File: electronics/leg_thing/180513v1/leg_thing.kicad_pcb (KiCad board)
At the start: 2 copper layers, 39.4 x 62.2 mm, 8 parts, among them J1 HIP, J2 THIGH, J3 KNEE, J4 CALF, U1 ESP32THINGPOWERSHIELD, U2 Teensy3.2_no_outer_inner

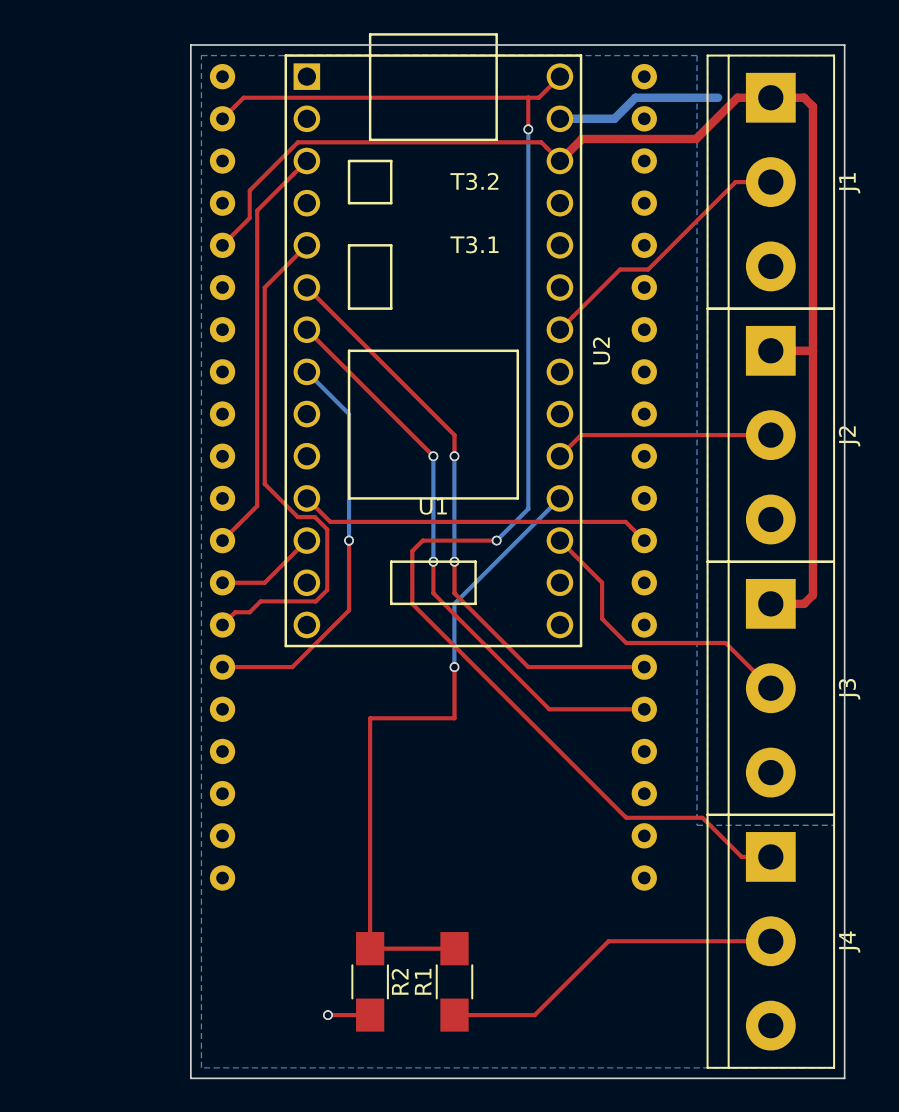
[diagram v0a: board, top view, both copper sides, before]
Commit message: reducing angular speed, setting max feet up to 1
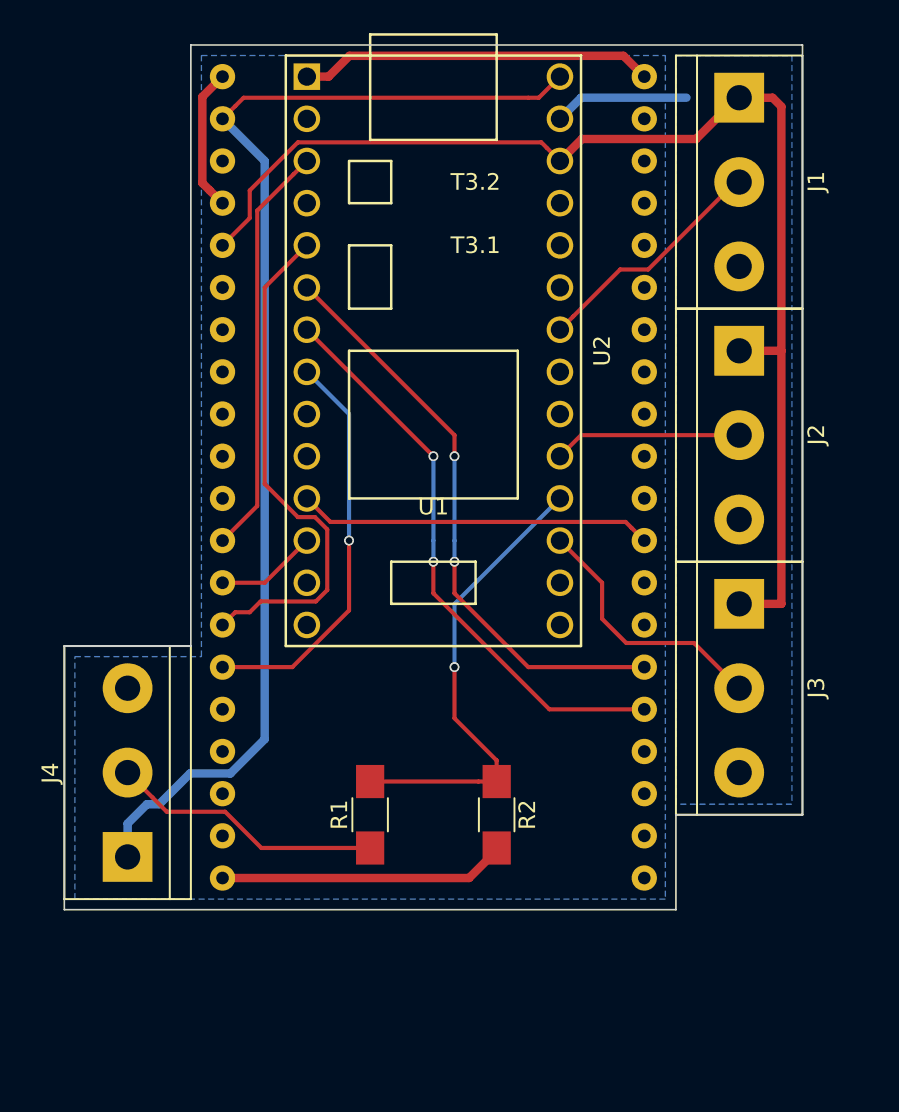
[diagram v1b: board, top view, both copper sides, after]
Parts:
- moved J4 38.7 mm to (95.9, 125.7), turned to 90 degrees
- moved R2 12.6 mm to (118.1, 123.2)
- moved R1 11.3 mm to (110.5, 123.2)
- moved J1 1.91 mm to (132.7, 80.0)
- moved J2 1.91 mm to (132.7, 95.2)
- moved J3 1.91 mm to (132.7, 110.5)
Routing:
- net GND: track 2.54 -> 47.3 mm, vias 1 -> 0
- net +5V: track 85.3 -> 72.2 mm, vias 2 -> 0
- net /CALFPOT3V3: track 39.9 -> 28.4 mm
- net /CALFPOT5V: track 20.9 -> 16.5 mm
- net /HIPPOT: track 16.4 -> 14.3 mm
- net /KNEEPOT: track 17.7 -> 15.8 mm
- net /THIGHPOT: track 13.2 -> 11.3 mm
- net GNDA: track 10.1 -> 8.15 mm
- net +3V3: track 76.1 -> 74.4 mm
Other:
- board size 39.4 x 62.2 mm -> 44.5 x 52.1 mm

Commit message: fixed esp32thingpowershield footprint, started new layout
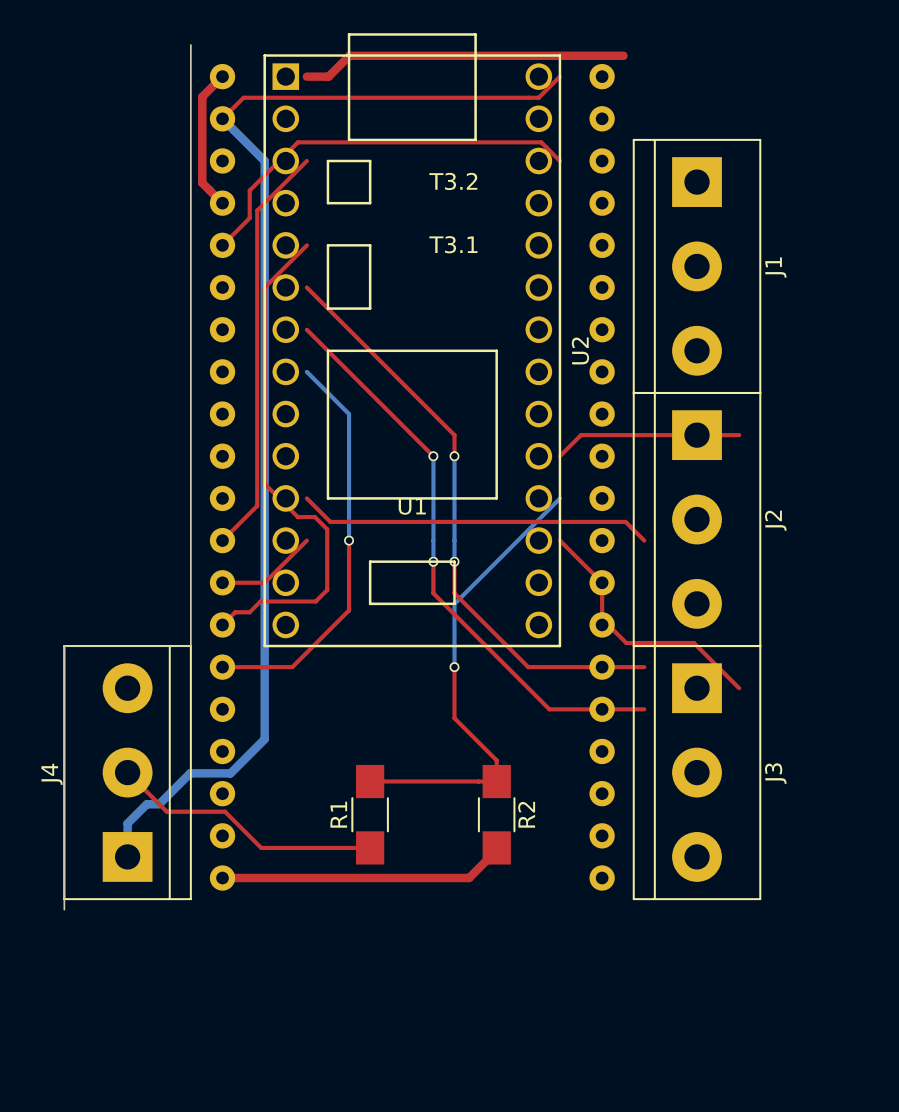
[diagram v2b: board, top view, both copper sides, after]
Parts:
- moved J1 5.68 mm to (130.2, 85.1)
- moved J2 5.68 mm to (130.2, 100.3)
- moved J3 5.68 mm to (130.2, 115.6)
- moved U1 1.27 mm to (113.0, 104.1)
- moved U2 1.27 mm to (113.0, 95.2)
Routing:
- net +3V3: track 74.4 -> 24.3 mm
- net /HIPPOT: track 14.3 -> 0.00 mm
- net (no net): track 0.00 -> 8.63 mm
- net GNDA: track 8.15 -> 0.00 mm
- net /KNEEPOT: track 15.8 -> 9.62 mm
- net GND: track 47.3 -> 43.1 mm
- removed copper zone on B.Cu, net GND
- removed copper zone on B.Cu, net GNDA
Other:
- board size 44.5 x 52.1 mm -> 7.6 x 52.1 mm

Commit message: electronics: switching to 6 pin molex connectors
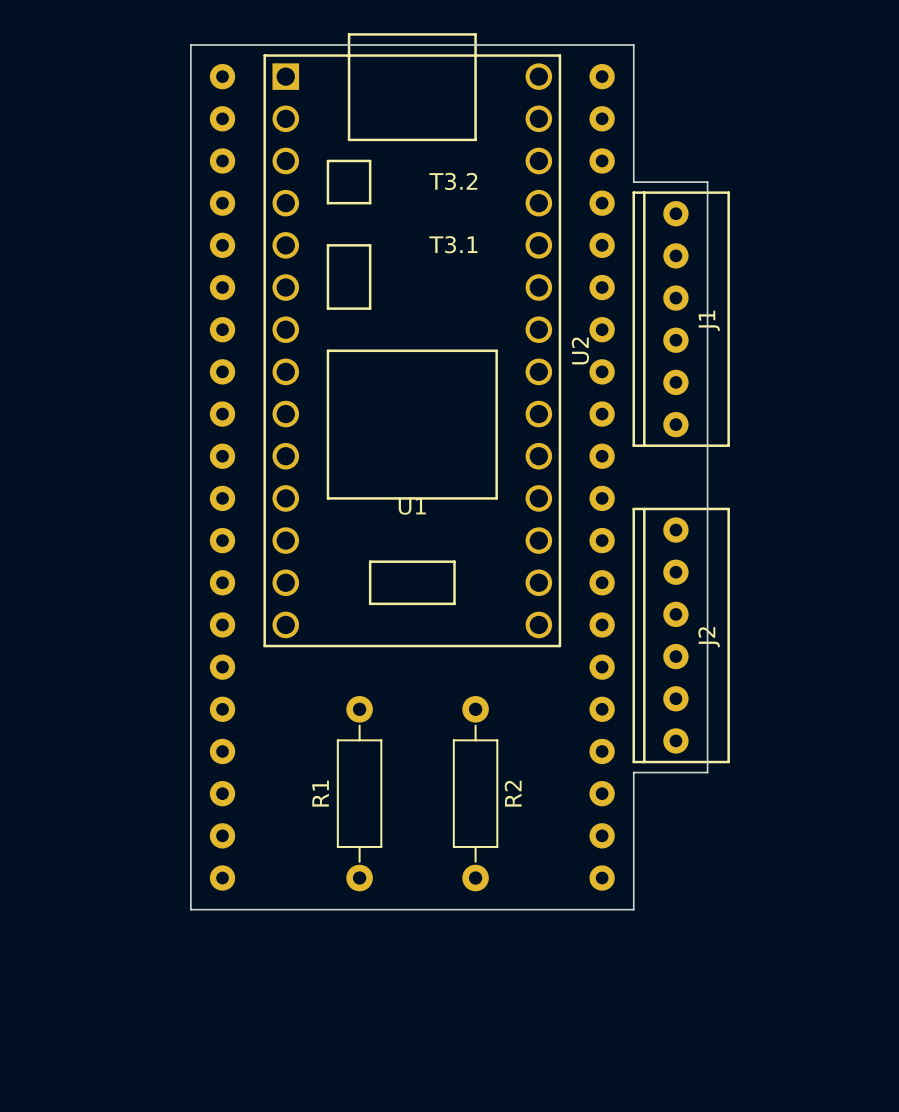
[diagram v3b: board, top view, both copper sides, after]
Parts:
- removed J3: KNEE, Connectors_Terminal_Blocks:TerminalBlock_bornier-3_P5.08mm
- removed J4: CALF, Connectors_Terminal_Blocks:TerminalBlock_bornier-3_P5.08mm
- J1: value HIP -> HIPCALF; footprint Connectors_Terminal_Blocks:TerminalBlock_bornier-3_P5.08mm -> leg_thing:MOLEX6PIN
- J2: value THIGH -> THIGHKNEE; footprint Connectors_Terminal_Blocks:TerminalBlock_bornier-3_P5.08mm -> leg_thing:MOLEX6PIN
- R1: value R -> 560; footprint Resistors_SMD:R_1206_HandSoldering -> Resistors_THT:R_Axial_DIN0207_L6.3mm_D2.5mm_P10.16mm_Horizontal
- R2: value R -> 1K; footprint Resistors_SMD:R_1206_HandSoldering -> Resistors_THT:R_Axial_DIN0207_L6.3mm_D2.5mm_P10.16mm_Horizontal
- moved J2 12.1 mm to (128.9, 112.4), turned to 0 degrees
- moved J1 8.35 mm to (128.9, 93.3), turned to 0 degrees
- moved R2 6.48 mm to (116.8, 116.8)
- moved R1 3.86 mm to (109.9, 127.0)
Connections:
- J1 pad 1: +3V3 -> GNDA
- J1 pad 3: GNDA -> +3V3
- J2 pad 2: /THIGHPOT -> GNDA
- J2 pad 3: GNDA -> /THIGHPOT
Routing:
- net +5V: track 72.2 -> 0.00 mm
- net GND: track 43.1 -> 0.00 mm
- net /THIGH1: track 35.4 -> 0.00 mm, vias 2 -> 0
- net /KNEE0: track 34.6 -> 0.00 mm, vias 2 -> 0
- net /THIGH0: track 31.2 -> 0.00 mm
- net /CALFPOT3V3: track 28.4 -> 0.00 mm, vias 1 -> 0
- net /MDISABLE: track 25.0 -> 0.00 mm
- net /KNEE1: track 24.5 -> 0.00 mm, vias 1 -> 0
- net +3V3: track 24.3 -> 0.00 mm
- net /HIP0: track 21.4 -> 0.00 mm
- net /CALFPOT5V: track 16.5 -> 0.00 mm
- net /THIGHPOT: track 11.3 -> 0.00 mm
- net /KNEEPOT: track 9.62 -> 0.00 mm
- net (no net): track 8.63 -> 0.00 mm
- net /HIP1: track 6.13 -> 0.00 mm
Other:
- board size 7.6 x 52.1 mm -> 31.1 x 52.1 mm

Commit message: electronics: finished layout with 6 pin molex
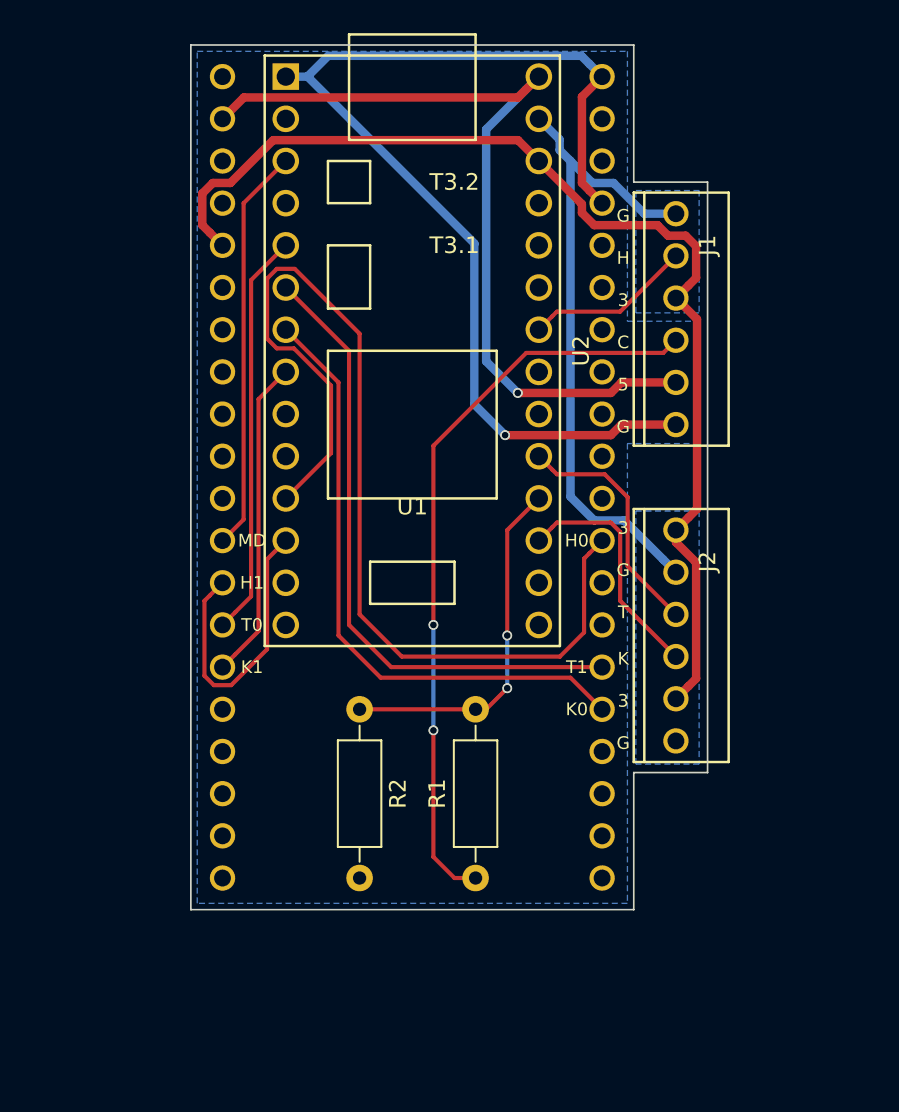
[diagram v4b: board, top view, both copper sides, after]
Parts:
- moved R1 6.98 mm to (116.8, 127.0)
- moved R2 6.98 mm to (109.9, 116.8)
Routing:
- net +3V3: track 0.00 -> 67.5 mm
- net GND: track 0.00 -> 65.8 mm, vias 0 -> 1
- net /HIP0: track 0.00 -> 62.1 mm
- net +5V: track 0.00 -> 51.0 mm, vias 0 -> 1
- net /CALFPOT5V: track 0.00 -> 45.1 mm, vias 0 -> 2
- net GNDA: track 0.00 -> 39.4 mm
- net /THIGH1: track 0.00 -> 38.2 mm
- net /KNEE0: track 0.00 -> 37.4 mm
- net /MDISABLE: track 0.00 -> 24.4 mm
- net /THIGH0: track 0.00 -> 24.4 mm
- net /CALFPOT3V3: track 0.00 -> 21.6 mm, vias 0 -> 2
- net /KNEE1: track 0.00 -> 19.4 mm
- net /HIP1: track 0.00 -> 18.0 mm
- net /THIGHPOT: track 0.00 -> 14.6 mm
- net /KNEEPOT: track 0.00 -> 14.5 mm
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- added copper zone on B.Cu, net GND
- added copper zone on B.Cu, net GNDA
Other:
- board text added: "3"
- board text added: "5"
- board text added: "C"
- board text added: "G"
- board text added: "H"
- board text added: "H0"
- board text added: "H1"
- board text added: "K"
- board text added: "K0"
- board text added: "K1"
- board text added: "MD"
- board text added: "T"
- board text added: "T0"
- board text added: "T1"

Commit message: adding pull-up resistor on disable line
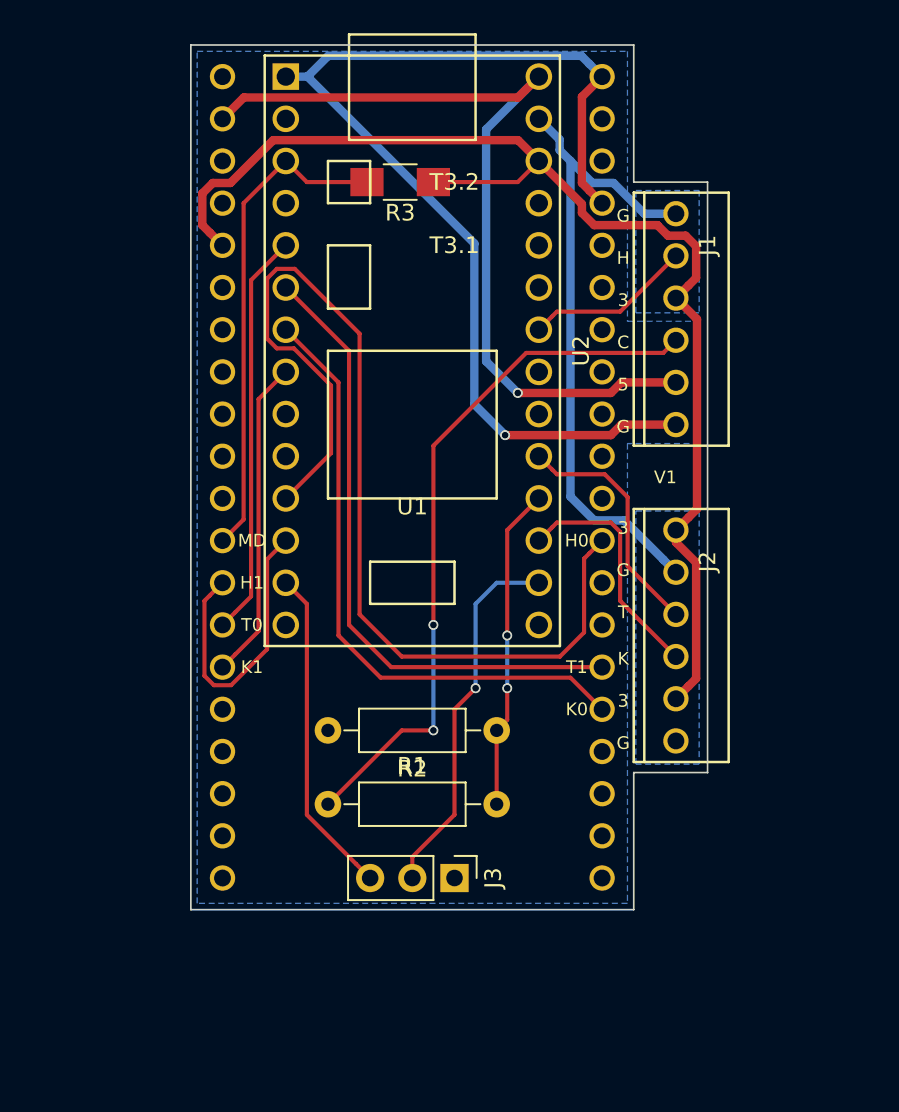
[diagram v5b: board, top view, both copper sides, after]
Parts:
- added J3: SPI, Pin_Headers:Pin_Header_Straight_1x03_Pitch2.54mm, F.Cu at (115.6, 127.0)
- added R3: 1K, Resistors_SMD:R_1206_HandSoldering, F.Cu at (112.3, 85.1)
- moved R1 9.94 mm to (108.0, 122.6), turned to 0 degrees
- moved R2 8.35 mm to (118.1, 118.1), turned to 180 degrees
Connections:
- U2 pad 13: Net-(U2-Pad13) -> /SPI_DO
- U2 pad 21: Net-(U2-Pad21) -> /SPI_CLK
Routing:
- net /SPI_CLK: track 0.00 -> 22.4 mm, vias 0 -> 1
- net /SPI_DO: track 0.00 -> 19.9 mm
- net +3V3: track 67.5 -> 74.3 mm
- net /MDISABLE: track 24.4 -> 29.9 mm
- net /CALFPOT5V: track 45.1 -> 42.6 mm
- net /CALFPOT3V3: track 21.6 -> 19.5 mm
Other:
- board text added: "V1"
